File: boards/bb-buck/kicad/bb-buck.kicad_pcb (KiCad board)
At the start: 2 copper layers, 40 x 30 mm, 26 parts, among them J1 KF128-5.08-2P, J2 KF128-5.08-2P, U1 LMR33630ADDAR

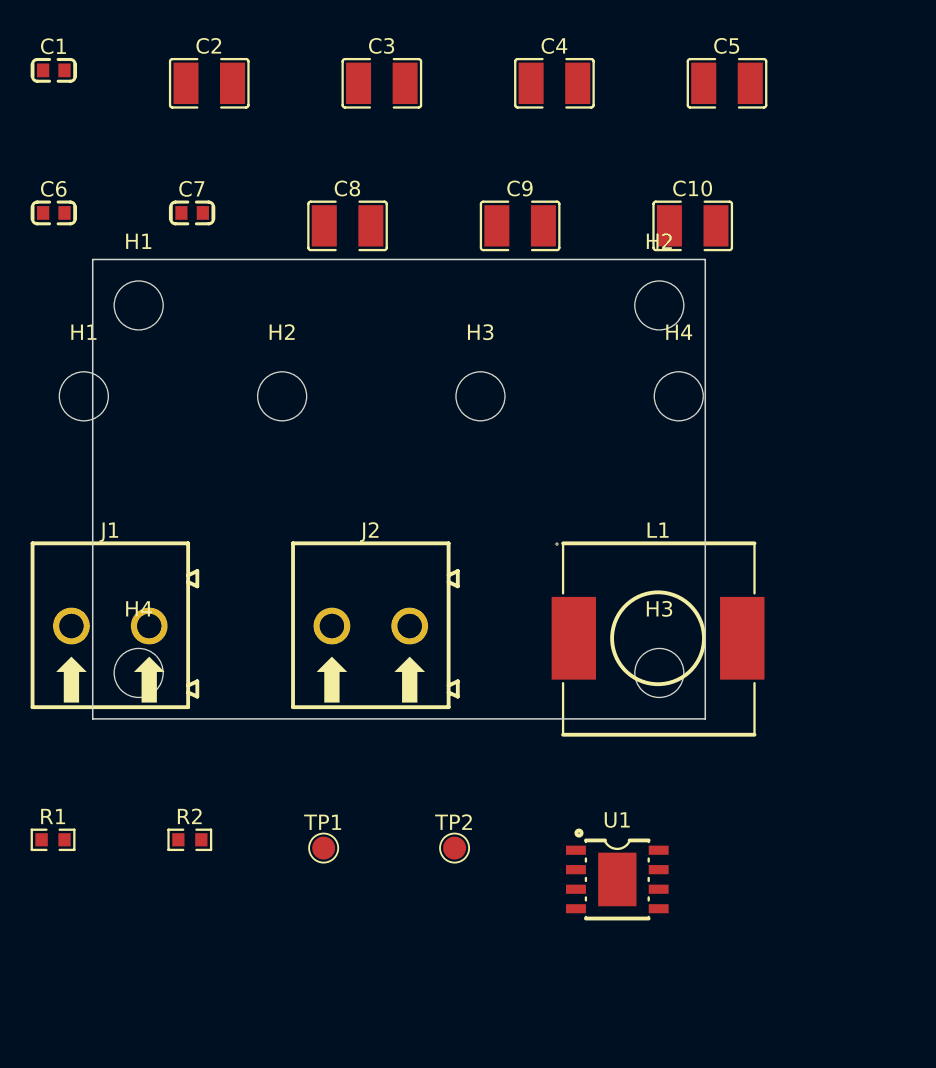
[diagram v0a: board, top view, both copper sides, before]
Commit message: ai-ee bb-buck: P5 board setup - outline cut to 35x25, parity 0
Owner directed a tight layout. Cut 40x30 -> 35x25 (1200 -> 875 mm2, -27%),
defensible because the thermal facts moved: H1's 1200 mm2 rested on the
placeholder 0.92 W against a 0.95 W gate; the real part is 0.76 W worst
case, and 875 mm2 keeps the pour above check_thermal's ~645 mm2 saturation
knee (~56 C rise vs the 70 C limit).

Mounting holes 4 -> 2 diagonal, freeing ~170 mm2 of corner keepout that the
hot loop and output bank need. Generator edited, schematic regenerated,
erc re-gated 0/0.

Corrected an owner premise by inspection, not by citing the doc: --outline
exists only on board_init.py and nothing else writes Edge.Cuts, so the edge
cut cannot be moved after placement. Strategy recorded: place -> measure ->
resize and RE-PLACE if slack -> route once at the final size.

board_init parity 0 (first run's 8 parity errors were duplicate mounting
holes from passing --mounting-holes over a schematic that already had them).
One residual: L1 overhangs the edge in the shelf-pack dump, a row-packer
artifact that P6 replaces wholesale.

rules_gen: netclasses split per IPC-2152 width - Pwr_0p56mm (+VIN) and
Pwr_1p52mm (/SW, +5V, GND). No flattening.

Co-Authored-By: Claude Opus 5 (1M context) <noreply@anthropic.com>
Claude-Session: https://claude.ai/code/session_011RYhfUJs4ynWvbR4LnpEFw
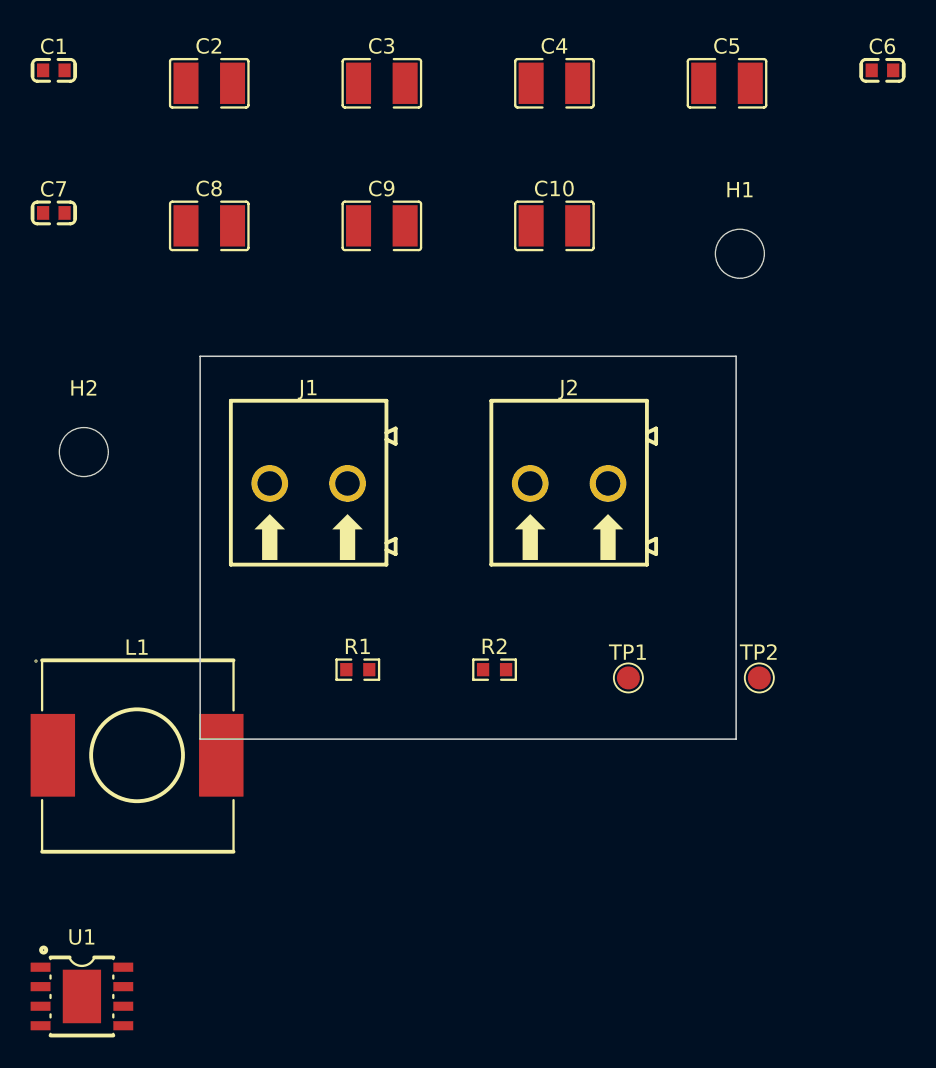
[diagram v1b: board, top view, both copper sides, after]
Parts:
- removed the H1 at (22.1, 31.2)
- removed the H1 at (18.5, 37.1)
- removed the H2 at (56.1, 31.2)
- removed the H2 at (31.4, 37.1)
- removed H3, H4: MountingHole_3.2mm_M3, MountingHole:MountingHole_3.2mm_M3
- removed H3, H4: M3_3.2mm, MountingHole:MountingHole_3.2mm_M3
- added H1: M3_3.2mm, MountingHole:MountingHole_3.2mm_M3, F.Cu at (61.3, 27.8)
- added H2: M3_3.2mm, MountingHole:MountingHole_3.2mm_M3, F.Cu at (18.5, 40.7)
- moved C6 54.9 mm to (70.6, 15.8)
- moved U1 35.8 mm to (18.4, 76.3)
- moved L1 34.9 mm to (21.9, 60.5)
- moved TP2 22.8 mm to (62.6, 55.5)
- moved R1 22.8 mm to (36.4, 54.9)
- moved R2 22.8 mm to (45.3, 54.9)
- moved TP1 22.8 mm to (54.0, 55.5)
- moved J1 15.9 mm to (33.2, 42.8)
- moved J2 15.9 mm to (50.2, 42.8)
- moved C9 9.03 mm to (37.9, 26.0)
- moved C10 9.03 mm to (49.2, 26.0)
- moved C7 9.03 mm to (16.5, 25.1)
- moved C8 9.03 mm to (26.7, 26.0)
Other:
- board size 40 x 30 mm -> 35 x 25 mm

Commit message: ai-ee bb-buck: P6 placement - place 0/0, probe 1.00, scrap averted on connectors
Both provisional screw-terminal rotations were WRONG (J1 0->270, J2 90->0).
The WRL carries (rotate 0 0 180) - the coincidence trap - so native entry
was resolved on a 3D test board and confirmed on orthographic renders. As
declared, both wire openings faced inward: unusable boards.

Hot loop hand-placed and LOCKED before anneal: C1 1.72 mm from both VIN and
PGND, pads uncrossed, ~2.2 mm2. All annealer candidates rejected on
structure (FB divider against L1's SW pad, probes outside the switch node);
the hand placement won on hpwl anyway, 125.0 vs 130.3+.

Outline FINAL at 35x25 by measurement: occupied 34.90x24.90, 0.05 mm slack
all round, fill 72.7%, largest empty rectangle 4x4 mm. No resize.

Toolchain fix: routelib's score regex crashed route_auto ON SUCCESS - the
zero-unrouted log line ends in a full stop that [\d.]+ swallowed, so
float() raised. Now \d+(?:\.\d+)?. Three prior boards never hit it because
they all had unrouted nets at probe time.

Also recorded (LEARNINGS + triage rows 301-303): planes_gen rejects the
_note convention while constraints_lint passes such a file, and two
placement constraint mechanisms silently do not enforce - keepouts are
never translated from board-local, and separation is centre-to-centre and
dropped when either ref is locked, which disabled all four pairs here.

Co-Authored-By: Claude Opus 5 (1M context) <noreply@anthropic.com>
Claude-Session: https://claude.ai/code/session_011RYhfUJs4ynWvbR4LnpEFw
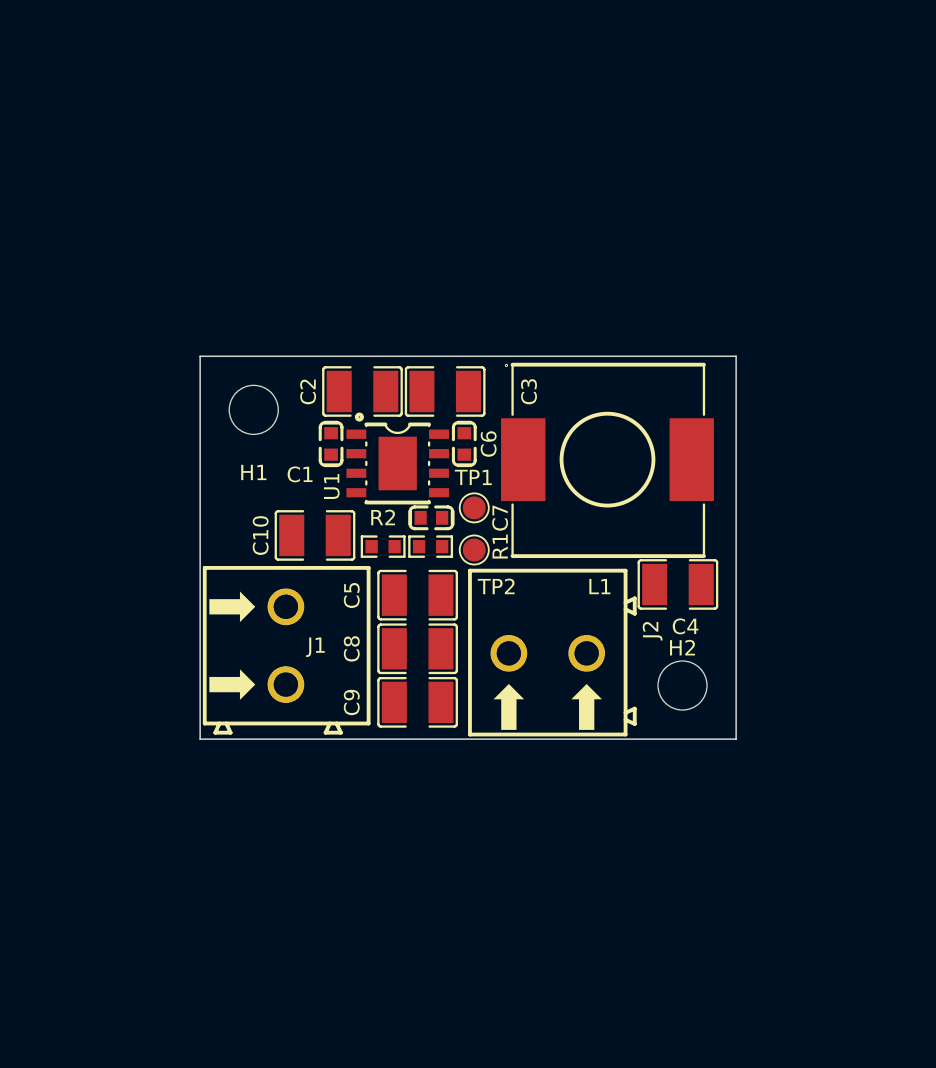
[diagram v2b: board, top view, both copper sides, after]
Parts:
- moved H2 42.0 mm to (57.6, 56.0)
- moved U1 40.5 mm to (39.0, 41.5)
- moved C5 39.1 mm to (40.3, 50.1)
- moved C6 36.6 mm to (43.3, 40.2), turned to 90 degrees
- moved L1 36.3 mm to (52.7, 41.2)
- moved C4 33.7 mm to (57.3, 49.4), turned to 180 degrees
- moved H1 33.3 mm to (29.6, 38.0)
- moved C7 31.7 mm to (41.2, 45.0), turned to 180 degrees
- moved C9 31.2 mm to (40.3, 57.1)
- moved C8 30.8 mm to (40.3, 53.6)
- moved C1 30.4 mm to (34.6, 40.2), turned to 90 degrees
- moved C10 25.6 mm to (33.6, 46.2), turned to 180 degrees
- moved C2 22.5 mm to (36.7, 36.8)
- moved C3 20.5 mm to (42.1, 36.8)
- moved TP2 20.4 mm to (44.0, 47.1)
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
